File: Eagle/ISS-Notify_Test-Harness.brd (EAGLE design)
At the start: 63.5 x 63.5 mm, 46 parts, among them J1 CON_USB-MICRO-ZX62D-B-5P8, Q1 NTR4501N-D, U1 ATMEGA32U4, U2 LTC1153CS8, U3 TPS63001, X1 8 MHz

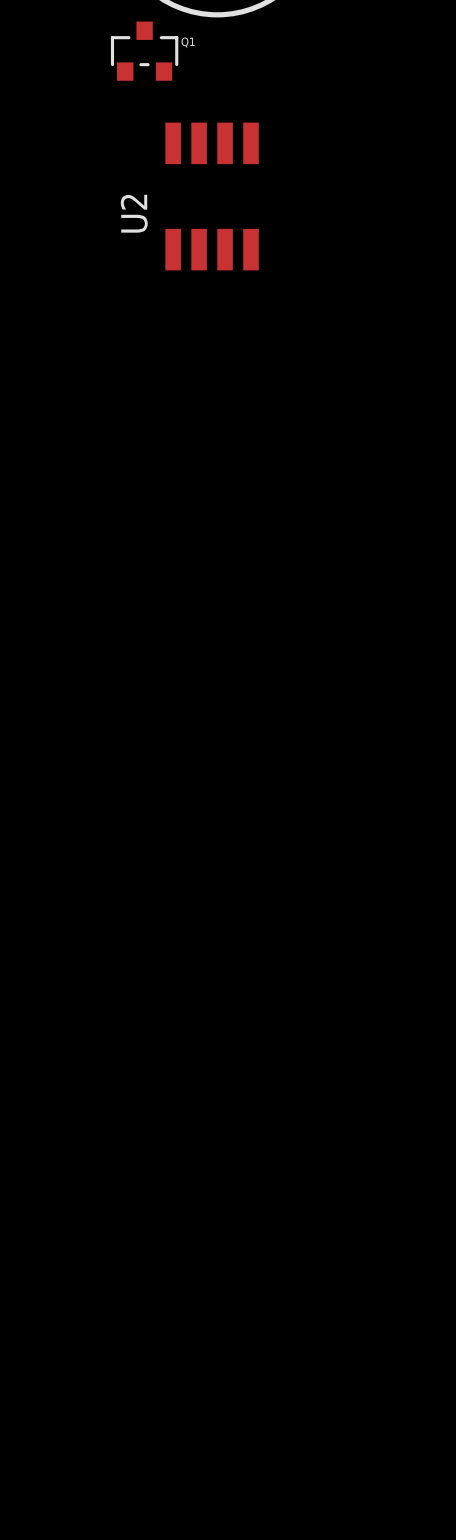
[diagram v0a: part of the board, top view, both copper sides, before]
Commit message: Added fiducials, added note about LTC1153 fuse circuit.
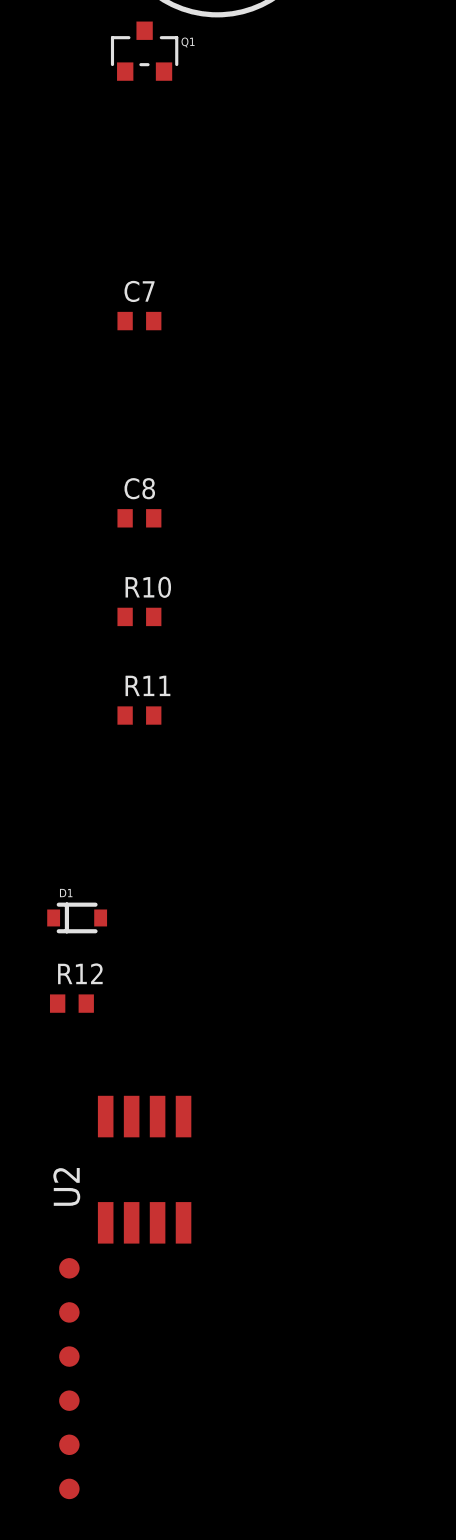
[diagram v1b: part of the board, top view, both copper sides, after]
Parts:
- added C7: 1 uF, rcl_custom:0603-C-NOSILK
- added C8: 0.1 uF, rcl_custom:0603-C-NOSILK
- added D1: 3.3V, SparkFun-DiscreteSemi:SOD-323
- added R10, R11: 1 k, rcl_custom:0603-C-NOSILK
- added R12: 1 ohm, rcl_custom:0603-C-NOSILK
- added U$10, U$5, U$6, U$7, U$8, U$9: FIDUCIAL, ISS-Notify:FIDUCIAL_1MM
- moved U2 47.7 mm to (0.25, -57.7)
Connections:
- new net FUSE_STATUS_UC: R10.1, R11.2, U1.1
- new net N$14: C7.2, U2.4
- new net N$15: U2.1
- new net N$16: C8.2, Q1.3, R12.1, U2.7
- new net N$17: R10.2, U2.3
- new net N$18: D1.C, Q1.1, U2.6
- new net N$19: D1.A, Q1.2
- net GND: now also R11.1, U2.5
- net N$13: now also C7.1, U2.2; no longer U1.1
- net TESTVCC: now also C8.1, R12.2, U2.8
- net VCC: no longer Q1.3
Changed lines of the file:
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@@
 <layer number="14" name="Route14" color="1" fill="6" visible="no" active="yes"/>
 <layer number="15" name="Route15" color="4" fill="6" visible="no" active="yes"/>
-<layer number="16" name="Bottom" color="1" fill="1" visible="yes" active="yes"/>
+<layer number="16" name="Bottom" color="1" fill="1" visible="no" active="yes"/>
 <layer number="17" name="Pads" color="2" fill="1" visible="yes" active="yes"/>
 <layer number="18" name="Vias" color="2" fill="1" visible="yes" active="yes"/>
@@
 <layer number="20" name="Dimension" color="15" fill="1" visible="yes" active="yes"/>
 <layer number="21" name="tPlace" color="7" fill="1" visible="yes" active="yes"/>
-<layer number="22" name="bPlace" color="7" fill="1" visible="yes" active="yes"/>
+<layer number="22" name="bPlace" color="7" fill="1" visible="no" active="yes"/>
 <layer number="23" name="tOrigins" color="15" fill="1" visible="yes" active="yes"/>
-<layer number="24" name="bOrigins" color="15" fill="1" visible="yes" active="yes"/>
+<layer number="24" name="bOrigins" color="15" fill="1" visible="no" active="yes"/>
 <layer number="25" name="tNames" color="7" fill="1" visible="yes" active="yes"/>
-<layer number="26" name="bNames" color="7" fill="1" visible="yes" active="yes"/>
+<layer number="26" name="bNames" color="7" fill="1" visible="no" active="yes"/>
 <layer number="27" name="tValues" color="7" fill="1" visible="no" active="yes"/>
 <layer number="28" name="bValues" color="7" fill="1" visible="no" active="yes"/>
@@
 <layer number="38" name="bTest" color="7" fill="1" visible="no" active="yes"/>
 <layer number="39" name="tKeepout" color="4" fill="11" visible="yes" active="yes"/>
-<layer number="40" name="bKeepout" color="1" fill="11" visible="yes" active="yes"/>
+<layer number="40" name="bKeepout" color="1" fill="11" visible="no" active="yes"/>
 <layer number="41" name="tRestrict" color="4" fill="10" visible="yes" active="yes"/>
-<layer number="42" name="bRestrict" color="1" fill="10" visible="yes" active="yes"/>
+<layer number="42" name="bRestrict" color="1" fill="10" visible="no" active="yes"/>
 <layer number="43" name="vRestrict" color="2" fill="10" visible="yes" active="yes"/>
 <layer number="44" name="Drills" color="7" fill="1" visible="no" active="yes"/>
@@
 <layer number="50" name="dxf" color="7" fill="1" visible="no" active="no"/>
 <layer number="51" name="tDocu" color="7" fill="1" visible="yes" active="yes"/>
-<layer number="52" name="bDocu" color="7" fill="1" visible="yes" active="yes"/>
+<layer number="52" name="bDocu" color="7" fill="1" visible="no" active="yes"/>
 <layer number="53" name="tGND_GNDA" color="7" fill="1" visible="no" active="no"/>
 <layer number="54" name="bGND_GNDA" color="7" fill="1" visible="no" active="no"/>
@@
 <layer number="112" name="tSilk" color="7" fill="1" visible="no" active="yes"/>
 <layer number="113" name="TEMP" color="7" fill="1" visible="yes" active="yes"/>
-<layer number="114" name="TEMP2" color="7" fill="1" visible="yes" active="yes"/>
+<layer number="114" name="TEMP2" color="7" fill="1" visible="no" active="yes"/>
 <layer number="116" name="Patch_BOT" color="7" fill="1" visible="no" active="yes"/>
 <layer number="121" name="_tsilk" color="7" fill="1" visible="no" active="yes"/>
@@
 <element name="Q1" library="max-viz" package="SOT-23" value="NTR4501N-D" x="0.254" y="-3.048"/>
 <element name="J1" library="ISS-Notify" package="USBMICROSMT-HIROSE" value="CON_USB-MICRO-ZX62D-B-5P8" x="1.651" y="17.907" rot="R270"/>
-<element name="U2" library="ISS-Notify" package="SO-8" value="LTC1153CS8" x="3.556" y="-10.033"/>
+<element name="C7" library="rcl_custom" package="0603-C-NOSILK" value="1 uF" x="0" y="-16.256"/>
+<element name="C8" library="rcl_custom" package="0603-C-NOSILK" value="0.1 uF" x="0" y="-25.908"/>
+<element name="R10" library="rcl_custom" package="0603-C-NOSILK" value="1 k" x="0" y="-30.734"/>
+<element name="R11" library="rcl_custom" package="0603-C-NOSILK" value="1 k" x="0" y="-35.56"/>
+<element name="D1" library="SparkFun-DiscreteSemi" package="SOD-323" value="3.3V" x="-3.048" y="-45.466">
+<attribute name="PROD_ID" value="DIO-11284" x="-3.048" y="-45.466" size="0.762" layer="27" display="off"/>
+</element>
+<element name="R12" library="rcl_custom" package="0603-C-NOSILK" value="1 ohm" x="-3.302" y="-49.657"/>
+<element name="U2" library="ISS-Notify" package="SO-8" value="LTC1153CS8" x="0.254" y="-57.658"/>
+<element name="U$5" library="ISS-Notify" package="FIDUCIAL_1MM" value="FIDUCIAL" x="-3.429" y="-62.611"/>
+<element name="U$6" library="ISS-Notify" package="FIDUCIAL_1MM" value="FIDUCIAL" x="-3.429" y="-64.77"/>
+<element name="U$7" library="ISS-Notify" package="FIDUCIAL_1MM" value="FIDUCIAL" x="-3.429" y="-66.929"/>
+<element name="U$8" library="ISS-Notify" package="FIDUCIAL_1MM" value="FIDUCIAL" x="-3.429" y="-69.088"/>
+<element name="U$9" library="ISS-Notify" package="FIDUCIAL_1MM" value="FIDUCIAL" x="-3.429" y="-71.247"/>
+<element name="U$10" library="ISS-Notify" package="FIDUCIAL_1MM" value="FIDUCIAL" x="-3.429" y="-73.406"/>
 </elements>
 <signals>
@@
 <contactref element="J1" pad="P$3"/>
 <contactref element="J1" pad="P$4"/>
+<contactref element="U2" pad="5"/>
+<contactref element="R11" pad="1"/>
+<wire x1="-0.7" y1="-35.56" x2="2.159" y2="-55.185" width="0" layer="19" extent="1-1"/>
+<wire x1="13.7" y1="2.2" x2="-0.7" y2="-35.56" width="0" layer="19" extent="1-1"/>
 </signal>
 <signal name="VCC">
@@
 <wire x1="62" y1="44.5" x2="59.55" y2="42.05" width="0.4064" layer="1"/>
 <wire x1="19.4" y1="41.7" x2="24" y2="37.8" width="0.6096" layer="1"/>
-<contactref element="Q1" pad="3"/>
-<wire x1="0.254" y1="-2.048" x2="25.592" y2="25.4" width="0" layer="19" extent="1-1"/>
 </signal>
 <signal name="D-">
@@
 <wire x1="60.54" y1="35.6" x2="60.5" y2="35.56" width="0.3048" layer="16"/>
 <contactref element="TESTVBAT" pad="1"/>
+<contactref element="C8" pad="1"/>
+<contactref element="R12" pad="2"/>
+<contactref element="U2" pad="8"/>
 <wire x1="50.5" y1="53.2" x2="44.5" y2="58.3" width="0" layer="19" extent="16-16"/>
+<wire x1="-0.7" y1="-25.908" x2="11.4" y2="33.9" width="0" layer="19" extent="1-1"/>
+<wire x1="-2.602" y1="-49.657" x2="-0.7" y2="-25.908" width="0" layer="19" extent="1-1"/>
+<wire x1="-1.651" y1="-55.185" x2="-2.602" y2="-49.657" width="0" layer="19" extent="1-1"/>
 </signal>
 <signal name="TESTSCLK">
@@
 </signal>
 <signal name="N$13">
+<contactref element="C7" pad="1"/>
+<contactref element="U2" pad="2"/>
+<wire x1="-0.7" y1="-16.256" x2="-0.381" y2="-60.385" width="0" layer="19" extent="1-1"/>
+</signal>
+<signal name="N$14">
+<contactref element="C7" pad="2"/>
+<contactref element="U2" pad="4"/>
+<wire x1="0.7" y1="-16.256" x2="2.159" y2="-60.385" width="0" layer="19" extent="1-1"/>
+</signal>
+<signal name="N$16">
+<contactref element="C8" pad="2"/>
+<contactref element="U2" pad="7"/>
+<contactref element="R12" pad="1"/>
+<contactref element="Q1" pad="3"/>
+<wire x1="-4.002" y1="-49.657" x2="-0.381" y2="-55.185" width="0" layer="19" extent="1-1"/>
+<wire x1="0.7" y1="-25.908" x2="-4.002" y2="-49.657" width="0" layer="19" extent="1-1"/>
+<wire x1="0.254" y1="-2.048" x2="0.7" y2="-25.908" width="0" layer="19" extent="1-1"/>
+</signal>
+<signal name="FUSE_STATUS_UC">
 <contactref element="U1" pad="1"/>
+<contactref element="R10" pad="1"/>
+<contactref element="R11" pad="2"/>
+<wire x1="-0.7" y1="-30.734" x2="25.75" y2="35.75" width="0" layer="19" extent="1-1"/>
+<wire x1="0.7" y1="-35.56" x2="-0.7" y2="-30.734" width="0" layer="19" extent="1-1"/>
+</signal>
+<signal name="N$18">
+<contactref element="Q1" pad="1"/>
+<contactref element="D1" pad="C"/>
+<contactref element="U2" pad="6"/>
+<wire x1="-4.198" y1="-45.466" x2="0.889" y2="-55.185" width="0" layer="19" extent="1-1"/>
+<wire x1="-0.696" y1="-4.048" x2="-4.198" y2="-45.466" width="0" layer="19" extent="1-1"/>
+</signal>
+<signal name="N$19">
+<contactref element="D1" pad="A"/>
+<contactref element="Q1" pad="2"/>
+<wire x1="1.204" y1="-4.048" x2="-1.898" y2="-45.466" width="0" layer="19" extent="1-1"/>
+</signal>
+<signal name="N$15">
+<contactref element="U2" pad="1"/>
+</signal>
+<signal name="N$17">
+<contactref element="U2" pad="3"/>
+<contactref element="R10" pad="2"/>
+<wire x1="0.7" y1="-30.734" x2="0.889" y2="-60.385" width="0" layer="19" extent="1-1"/>
 </signal>
 </signals>
-<errors>
-</errors>
 </board>
 </drawing>

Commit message: Harness passes ERC, DRC, rats. Ready for review. D1 part number not finalized.
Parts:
- removed U$10, U$5, U$6, U$7, U$8, U$9: FIDUCIAL, ISS-Notify:FIDUCIAL_1MM
- added F1, F2, F3, F4, F5, F6: FIDUCIAL, ISS-Notify:FIDUCIAL_1MM
- added R13: 51k, rcl_custom:0603-C-NOSILK
- moved U2 118.1 mm to (26.7, 57.4), turned to 270 degrees
- moved R12 114.3 mm to (33.0, 58.7), turned to 90 degrees
- moved D1 104.0 mm to (34.8, 51.4)
- moved C8 91.5 mm to (34.9, 58.7), turned to 270 degrees
- moved R11 88.9 mm to (18.3, 51.4)
- moved R10 84.9 mm to (21.2, 51.4)
- moved C7 76.5 mm to (21.1, 57.3), turned to 270 degrees
- moved Q1 67.4 mm to (34.8, 54.9)
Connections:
- net FUSE_STATUS_UC renamed !FUSE_STATUS_UC
- removed net N$14: C7.2, U2.4
- removed net N$15: U2.1
- removed net N$17: R10.2, U2.3
- new net !STATUS: R10.2, R13.1, U2.3
- net GND: now also C7.2, U1.42, U2.4
- net N$19: now also TESTVBAT.1
- net TESTVCC: no longer C8.1, R12.2, TESTVBAT.1, U2.8
- net VIN: now also C8.1, R12.2, R13.2, U2.1, U2.8
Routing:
- net VIN: track 63.9 -> 114.0 mm
- net !FUSE_STATUS_UC: track 0.00 -> 21.0 mm, vias 0 -> 2
- net N$19: track 0.00 -> 14.9 mm
- net !STATUS: track 0.00 -> 12.4 mm
- net N$18: track 0.00 -> 8.89 mm
- net N$16: track 0.00 -> 7.97 mm
- net N$13: track 0.00 -> 2.89 mm
- net GND: vias 50 -> 52

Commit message: Ordered this board so it'd better be right.
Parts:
- D1: value 3.3V -> 6V
- R12: value 1 ohm -> 250 milliohms
- moved TESTGND 3.68 mm to (39.4, 61.0)
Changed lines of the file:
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@@
 <attribute name="NAME" x="28.7" y="47.8" size="0.762" layer="25" font="vector" ratio="20"/>
 </element>
-<element name="TESTGND" library="ISS-Notify" package="POGOPIN" value="POGOPIN" x="41.91" y="58.293" smashed="yes">
-<attribute name="NAME" x="42.386" y="52.102" size="0.762" layer="25" font="vector" ratio="20" rot="R90"/>
+<element name="TESTGND" library="ISS-Notify" package="POGOPIN" value="POGOPIN" x="39.37" y="60.96" smashed="yes">
+<attribute name="NAME" x="39.846" y="54.769" size="0.762" layer="25" font="vector" ratio="20" rot="R90"/>
 </element>
 <element name="TESTMISO" library="ISS-Notify" package="POGOPIN" value="POGOPIN" x="13.95" y="33.9" smashed="yes"/>
@@
 <attribute name="VALUE" x="17.488" y="49.435" size="1" layer="27" ratio="10"/>
 </element>
-<element name="D1" library="SparkFun-DiscreteSemi" package="SOD-323" value="3.3V" x="34.798" y="51.435" smashed="yes">
+<element name="D1" library="SparkFun-DiscreteSemi" package="SOD-323" value="6V" x="34.798" y="51.435" smashed="yes">
 <attribute name="PROD_ID" value="DIO-11284" x="34.798" y="51.435" size="0.762" layer="27" display="off"/>
 <attribute name="NAME" x="34.163" y="49.53" size="0.762" layer="25" font="vector" ratio="20"/>
 <attribute name="VALUE" x="33.782" y="50.038" size="0.4064" layer="27"/>
 </element>
-<element name="R12" library="rcl_custom" package="0603-C-NOSILK" value="1 ohm" x="33.02" y="58.674" smashed="yes" rot="R90">
+<element name="R12" library="rcl_custom" package="0603-C-NOSILK" value="250 milliohms" x="33.02" y="58.674" smashed="yes" rot="R90">
 <attribute name="NAME" x="31.303" y="59.728" size="0.762" layer="25" font="vector" ratio="20" rot="R270"/>
 <attribute name="VALUE" x="35.02" y="57.874" size="1" layer="27" ratio="10" rot="R90"/>
@@
 </signal>
 </signals>
-<errors>
-</errors>
 </board>
 </drawing>
